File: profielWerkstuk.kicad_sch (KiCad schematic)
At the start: 75 parts, among them Q1 2N5179, SW1 SW_HF/VHF, SW2 SW_ANT, SW3 SW_PRESELECT_HFa, SW4 SW_PRESELECT_VHFa, SW5 SW_PRESELECT_HFb, SW6 SW_PRESELECT_VHFb

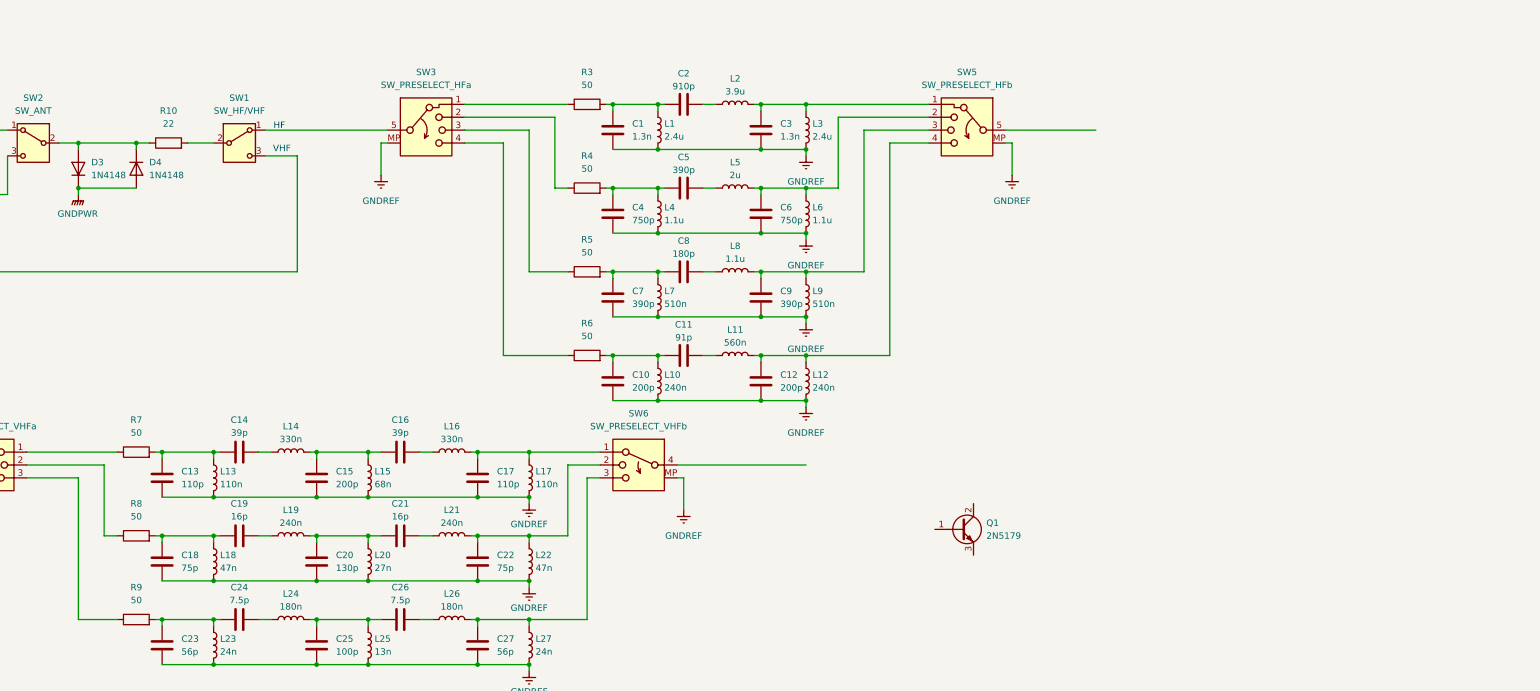
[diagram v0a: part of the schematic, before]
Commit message: added mixer
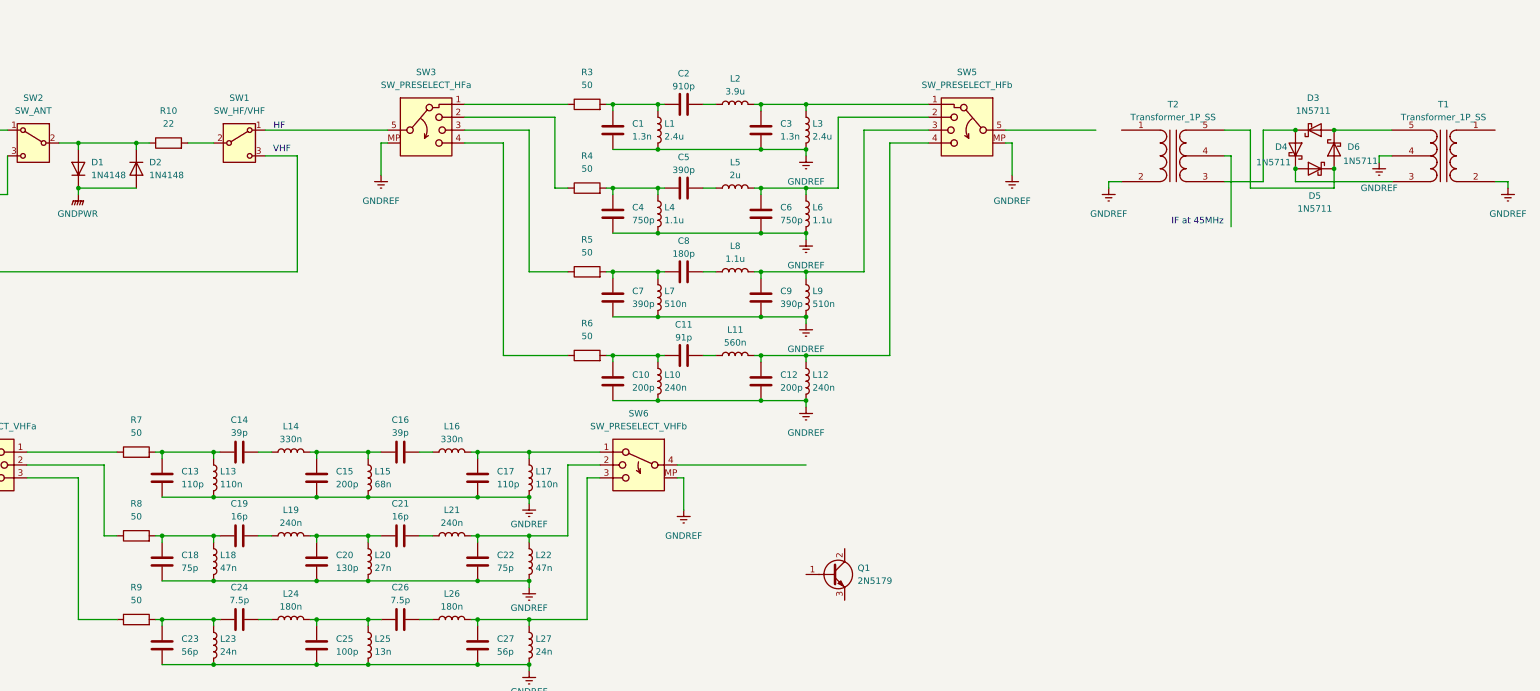
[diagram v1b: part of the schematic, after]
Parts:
- added D3, D4, D5, D6: 1N5711, Diode_THT:D_DO-35_SOD27_P7.62mm_Horizontal, symbol Diode:1N5711
- added T1, T2: Transformer_1P_SS, symbol Device:Transformer_1P_SS
- renumbered D3 to D1, D4 to D2
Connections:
- net GNDREF: now also T1.2 (AB), T1.4 (SC), T2.2 (AB)
- new net: D4.1 (K), D5.2 (A), T1.3 (SA)
- new net: D3.2 (A), D6.1 (K), T1.5 (SB)
- new net: D3.1 (K), D4.2 (A), T2.3 (SA)
- new net: D5.1 (K), D6.2 (A), T2.5 (SB)
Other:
- note added: "IF at 45MHz"
- moved on the sheet: Q1

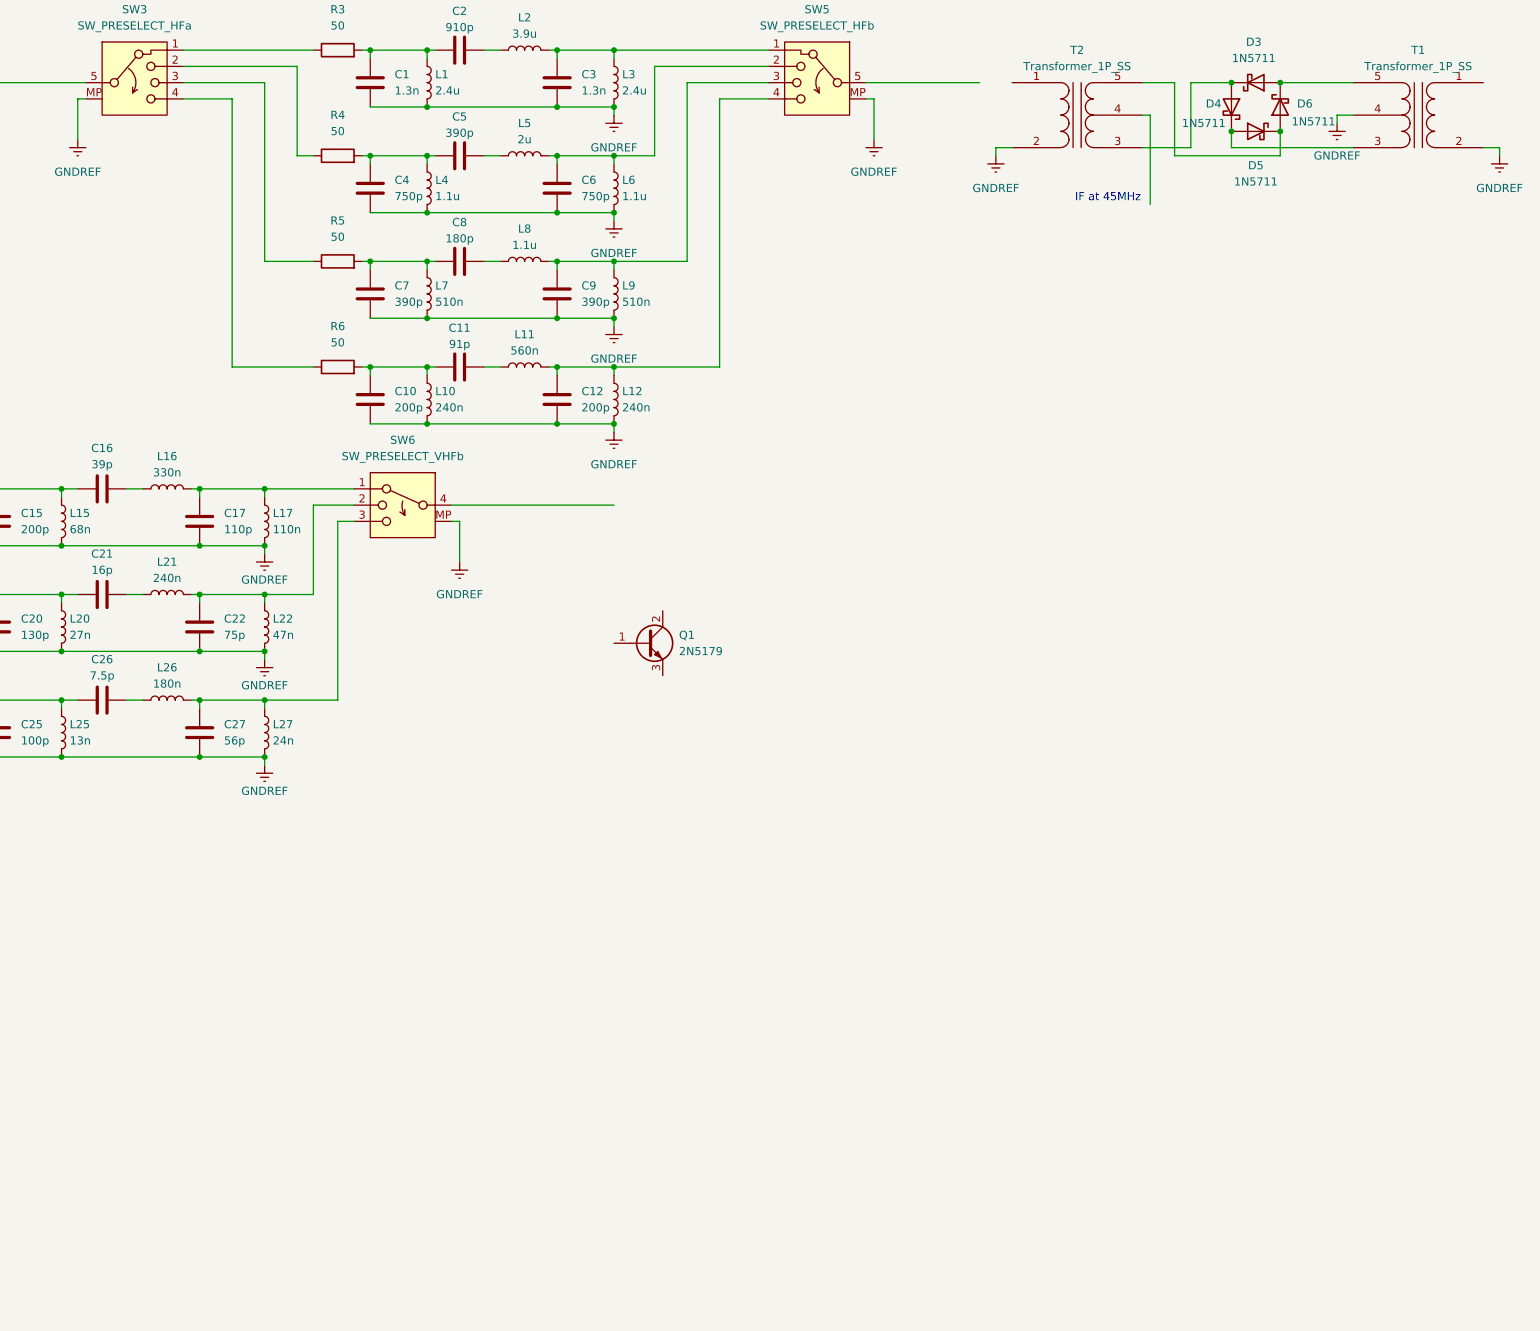
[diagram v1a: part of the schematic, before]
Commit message: added a AM demod
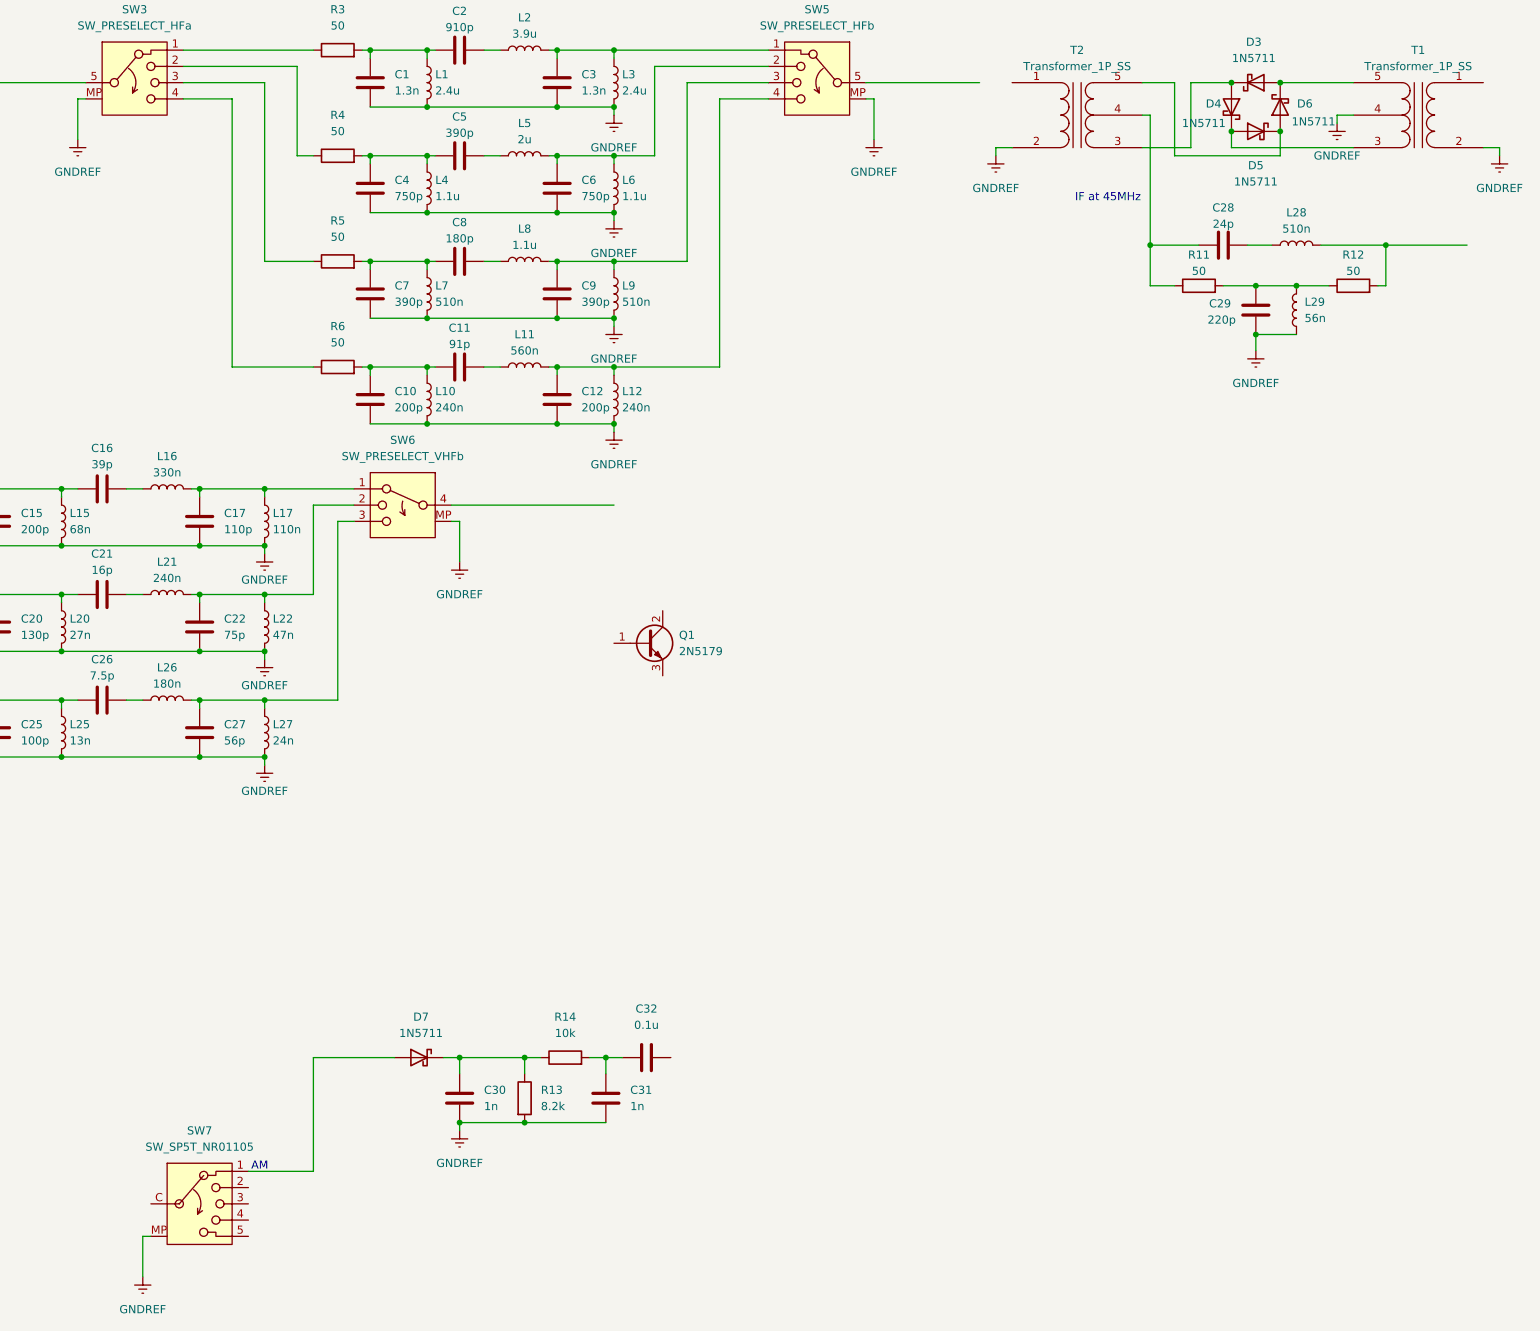
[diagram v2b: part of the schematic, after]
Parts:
- added C28: 24p, symbol Device:C
- added C29: 220p, symbol Device:C
- added C30, C31: 1n, symbol Device:C
- added C32: 0.1u, symbol Device:C
- added D7: 1N5711, Diode_THT:D_DO-35_SOD27_P7.62mm_Horizontal, symbol Diode:1N5711
- added L28: 510n, symbol Device:L
- added L29: 56n, symbol Device:L
- added R11, R12: 50, symbol Device:R
- added R13: 8.2k, symbol Device:R
- added R14: 10k, symbol Device:R
- added SW7: SW_SP5T_NR01105, Button_Switch_THT:SW_NKK_NR01, symbol Switch:SW_SP5T_NR01105
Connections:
- net GNDREF: now also C29.1, C30.2, C31.2, L29.1, R13.2, SW7.MP
- net at T2.4 (SC): now also C28.1, R11.1
- new net: C29.2, L29.2, R11.2, R12.1
- new net: C30.1, D7.1 (K), R13.1, R14.1
- new net: C31.1, C32.1, R14.2
- new net: C28.2, L28.1
- new net: L28.2, R12.2
- new net: D7.2 (A), SW7.1
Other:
- note added: "AM"

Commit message: did some organization
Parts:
- removed SW7: SW_SP5T_NR01105, Button_Switch_THT:SW_NKK_NR01, symbol Switch:SW_SP5T_NR01105
- added D10, D11, D8, D9: 1N5711, Diode_THT:D_DO-35_SOD27_P7.62mm_Horizontal, symbol Diode:1N5711
- added T4, T5: Transformer_1P_SS, symbol Device:Transformer_1P_SS
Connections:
- net GNDREF: now also T4.2 (AB), T5.2 (AB), T5.4 (SC)
- new net: D8.2 (A), D9.1 (K), T4.3 (SA)
- new net: D11.1 (K), D9.2 (A), T5.5 (SB)
- new net: D10.1 (K), D11.2 (A), T4.5 (SB)
- new net: D10.2 (A), D8.1 (K), T5.3 (SA)
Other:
- note removed: "AM"
- moved on the sheet: C30, C31, C32, D7, R13, R14

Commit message: added filter or smth
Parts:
- added C33: 15p, symbol Device:C
- added C34: 130p, symbol Device:C
- added C35, C37: 100p, symbol Device:C
- added C36, C38: 910p, symbol Device:C
- added D16, D17, D18, D19, D20, D21, D22, D23, D24, D25, D26, D27: 1N5711, Diode_THT:D_DO-35_SOD27_P7.62mm_Horizontal, symbol Diode:1N5711
- added L30: 330n, symbol Device:L
- added L31: 39n, symbol Device:L
- added L32, L34: 2200n, symbol Device:L
- added L33, L35: 240n, symbol Device:L
- added R15, R16, R17, R18, R19, R20: 50, symbol Device:R
- added T10, T11, T12, T3, T8, T9: Transformer_1P_SS, symbol Device:Transformer_1P_SS
- added XF1: ECS-45K30A, symbol filterbieb:XF
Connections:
- net GNDREF: now also C34.1, C36.1, C38.1, L31.1, L33.1, L35.1, T10.2 (AB), T10.4 (SC), T11.2 (AB), T12.2 (AB), T12.4 (SC), T3.2 (AB), T8.2 (AB), T8.4 (SC), T9.2 (AB), XF1.2 (gnd)
- new net: C37.1, R19.1, T11.4 (SC)
- new net: C37.2, L34.1
- new net: D26.1 (K), D27.2 (A), T11.5 (SB)
- new net: D24.1 (K), D26.2 (A), T12.3 (SA)
- new net: C38.2, L35.2, R19.2, R20.1
- new net: L34.2, R20.2
- new net: C33.1, R15.1, T3.4 (SC)
- new net: C33.2, L30.1
- new net: D25.2 (A), D27.1 (K), T12.5 (SB)
- new net: D24.2 (A), D25.1 (K), T11.3 (SA)
- new net: C34.2, L31.2, R15.2, R16.1
- new net: D17.2 (A), D19.1 (K), T8.5 (SB)
- new net: D18.1 (K), D19.2 (A), T3.5 (SB)
- new net: C35.1, R17.1, T9.4 (SC)
- new net: C35.2, L32.1
- new net: C36.2, L33.2, R17.2, R18.1
- new net: D20.1 (K), D22.2 (A), T10.3 (SA)
- new net: D20.2 (A), D21.1 (K), T9.3 (SA)
- new net: D22.1 (K), D23.2 (A), T9.5 (SB)
- new net: L30.2, R16.2
- new net: D21.2 (A), D23.1 (K), T10.5 (SB)
- new net: D16.2 (A), D17.1 (K), T3.3 (SA)
- new net: L32.2, R18.2
- new net: D16.1 (K), D18.2 (A), T8.3 (SA)
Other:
- note added: "IF at 10.7MHz"
- note added: "IF at 455KHz"
- note added: "IF at 70MHz"
- moved on the sheet: D10, D11, D8, D9, T4, T5

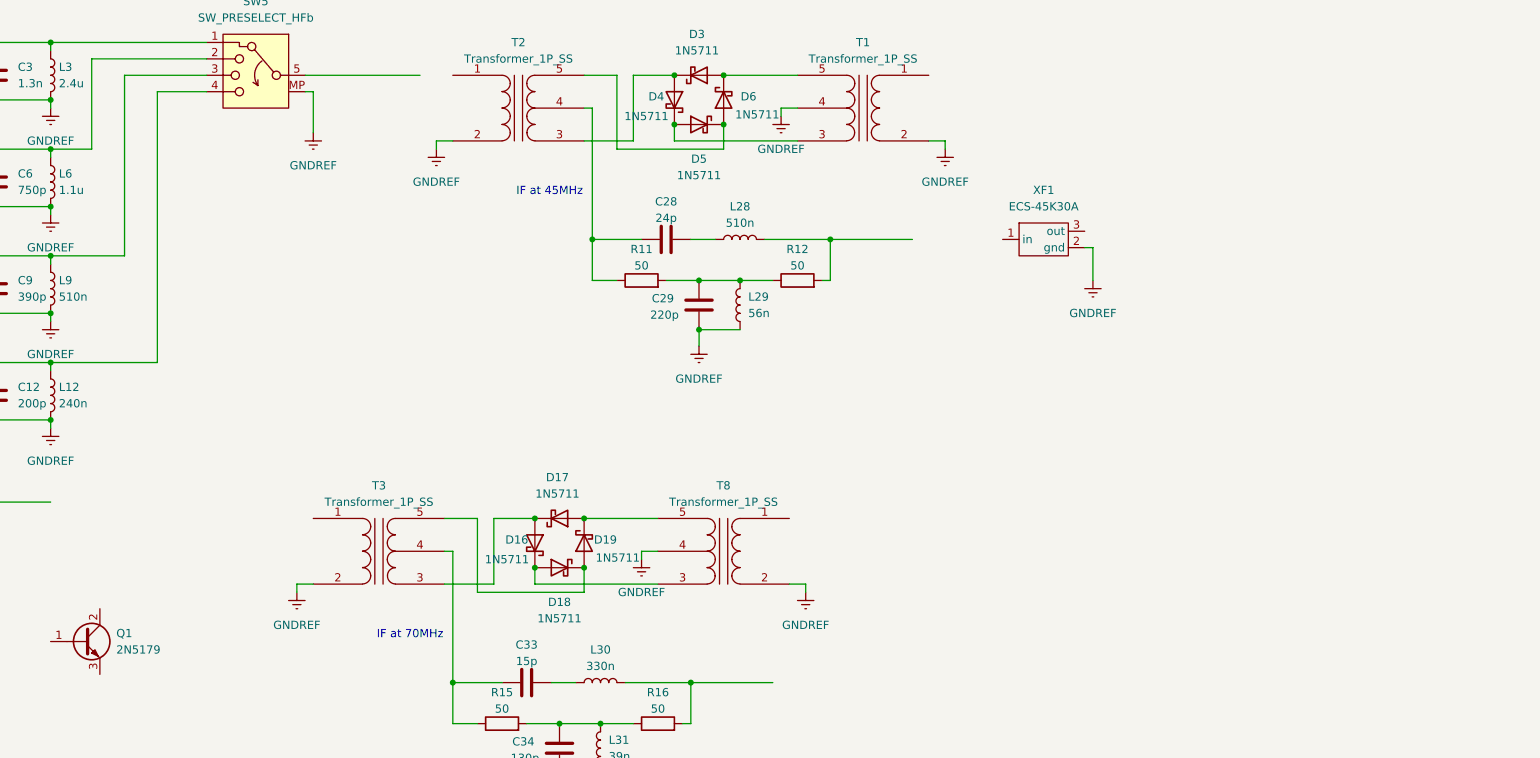
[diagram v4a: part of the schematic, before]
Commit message: added filter and transistor for amplifier
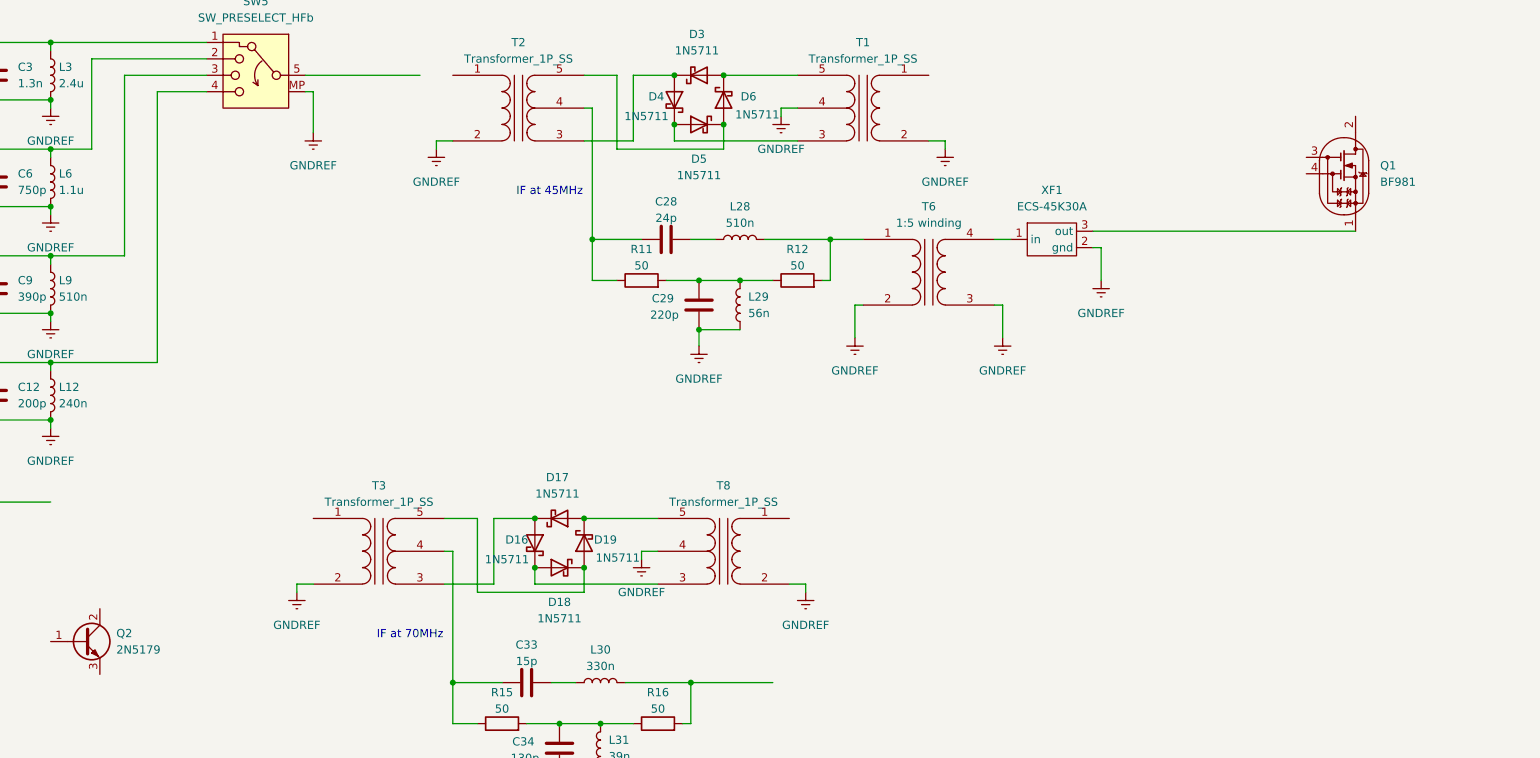
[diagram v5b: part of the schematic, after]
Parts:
- added Q1: BF981, Package_TO_SOT_SMD:SOT-143, symbol Transistor_FET:BF994S
- added T6: 1:5 winding, symbol Device:Transformer_1P_1S
- renumbered Q1 to Q2
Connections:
- net GNDREF: now also T6.2 (AB), T6.3 (SA)
- net at L28.2, R12.2: now also T6.1 (AA)
- net at XF1.1 (in): now also T6.4 (SB)
- net at XF1.3 (out): now also Q1.1 (S)
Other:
- moved on the sheet: XF1
